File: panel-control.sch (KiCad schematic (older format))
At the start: 65 parts, among them J1 POWER_CONN, J10 PWR_HAT, J11 BOOT, J2 PROG, J3 PWR, J4 40HAT, J5 HUB-75_A, J6 HUB-75_B, J7 USB_PWR, J8 FAN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

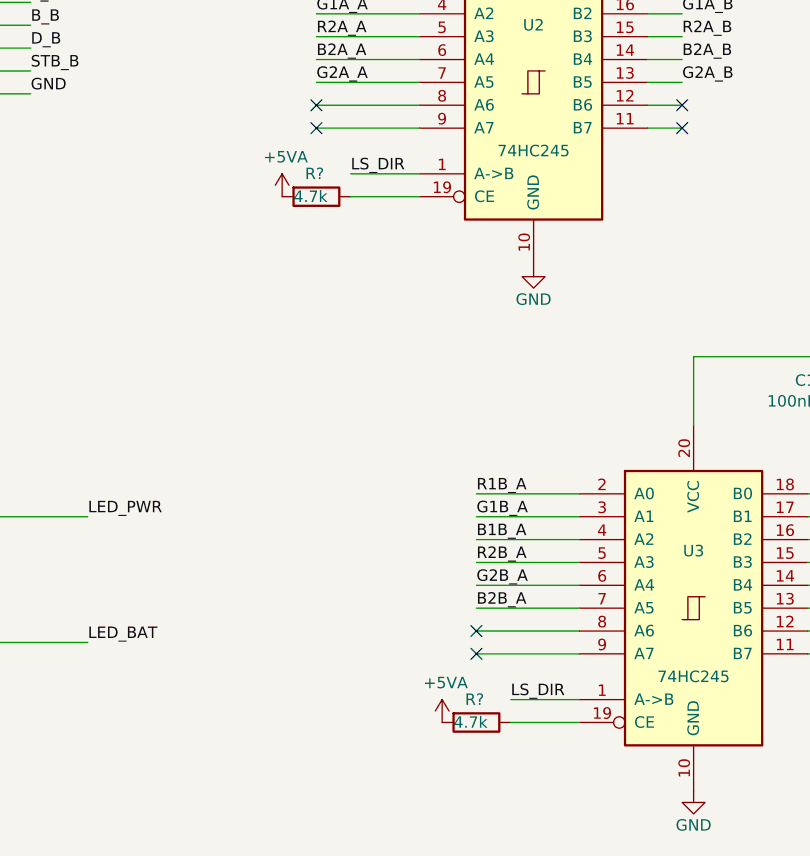
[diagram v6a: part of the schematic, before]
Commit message: annotate sch
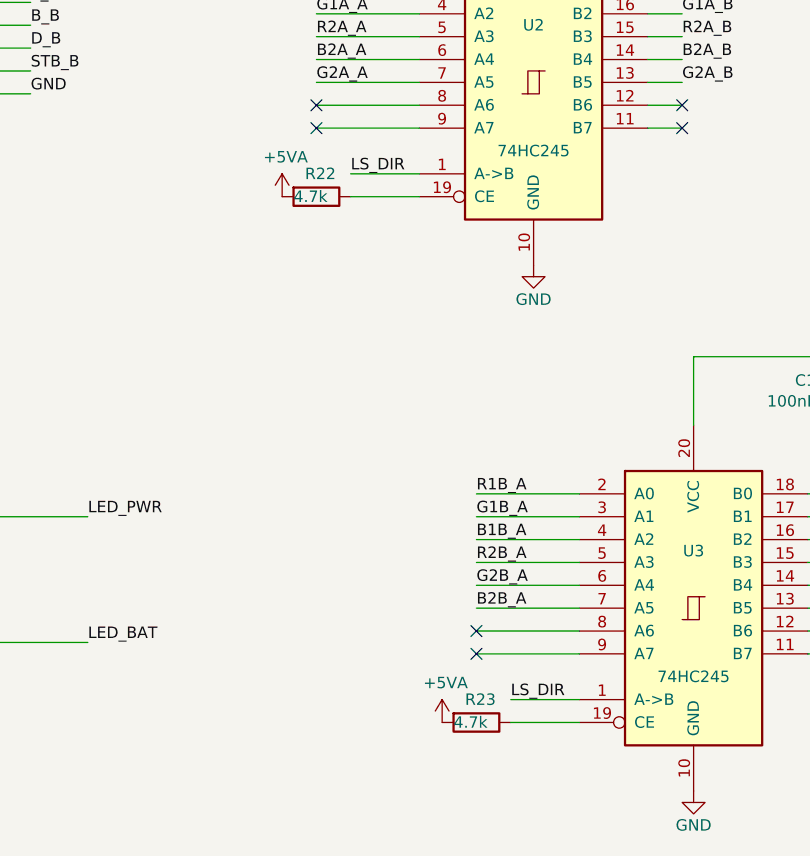
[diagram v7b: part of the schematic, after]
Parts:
- gave numbers to parts that had none: 2
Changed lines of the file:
@@
 LS_DIR
 $Comp
-L Device:R R?
+L Device:R R22
 U 1 1 617C81C2
 P 6600 7750
-F 0 "R?" V 6500 7700 50  0000 L CNN
+F 0 "R22" V 6500 7700 50  0000 L CNN
 F 1 "4.7k" V 6600 7650 50  0000 L CNN
 F 2 "Resistor_SMD:R_0402_1005Metric" V 6530 7750 50  0001 C CNN
@@
 $EndComp
 $Comp
-L power:+5VA #PWR?
+L power:+5VA #PWR09
 U 1 1 617CEDFD
 P 6450 7750
-F 0 "#PWR?" H 6450 7600 50  0001 C CNN
+F 0 "#PWR09" H 6450 7600 50  0001 C CNN
 F 1 "+5VA" H 6465 7923 50  0000 C CNN
 F 2 "" H 6450 7750 50  0001 C CNN
@@
 $EndComp
 $Comp
-L Device:R R?
+L Device:R R23
 U 1 1 617DA57C
 P 7300 10050
-F 0 "R?" V 7200 10000 50  0000 L CNN
+F 0 "R23" V 7200 10000 50  0000 L CNN
 F 1 "4.7k" V 7300 9950 50  0000 L CNN
 F 2 "Resistor_SMD:R_0402_1005Metric" V 7230 10050 50  0001 C CNN
@@
 $EndComp
 $Comp
-L power:+5VA #PWR?
+L power:+5VA #PWR011
 U 1 1 617DA582
 P 7150 10050
-F 0 "#PWR?" H 7150 9900 50  0001 C CNN
+F 0 "#PWR011" H 7150 9900 50  0001 C CNN
 F 1 "+5VA" H 7165 10223 50  0000 C CNN
 F 2 "" H 7150 10050 50  0001 C CNN
